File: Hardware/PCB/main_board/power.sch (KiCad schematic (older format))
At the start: 8 parts, among them J4 USB_B

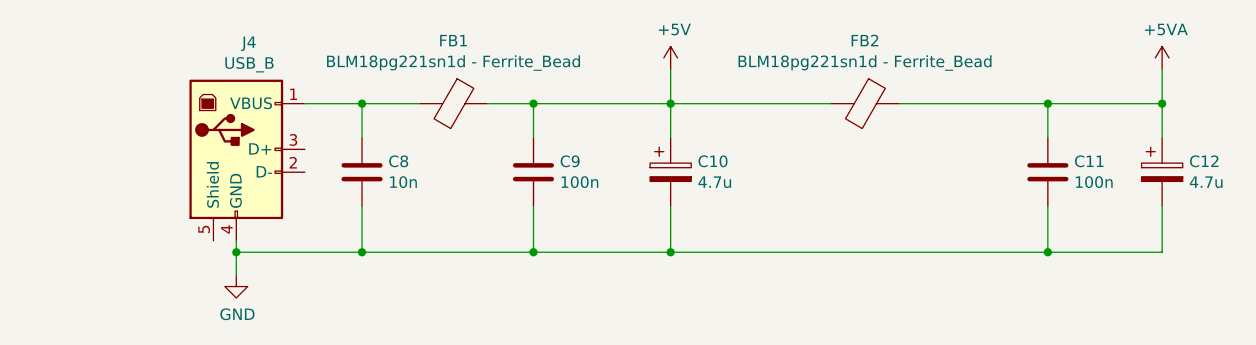
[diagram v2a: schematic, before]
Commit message: Update 3D view
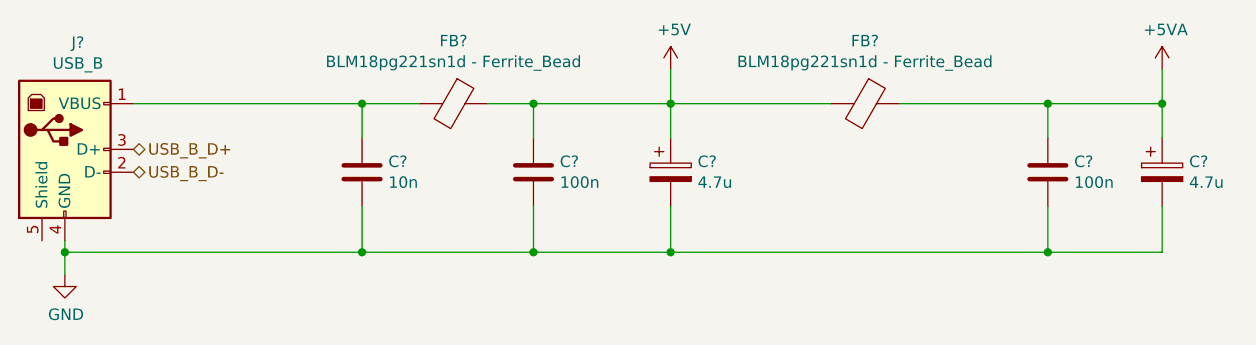
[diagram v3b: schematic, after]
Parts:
- renumbered C8 to C?, C9 to C?, C10 to C?, C11 to C?, C12 to C?, FB1 to FB?, FB2 to FB?, J4 to J?
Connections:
- net USB_B_D-: now reaches J?.2 (D-)
- net USB_B_D+: now reaches J?.3 (D+)
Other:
- moved on the sheet: J?
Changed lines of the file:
@@
 $Descr A4 11693 8268
 encoding utf-8
-Sheet 5 7
+Sheet 3 7
 Title ""
 Date ""
@@
 $EndDescr
 $Comp
-L power:GND #PWR09
+L power:GND #PWR?
 U 1 1 5E57CDA6
-P 2650 3650
-F 0 "#PWR09" H 2650 3400 50  0001 C CNN
-F 1 "GND" H 2655 3477 50  0000 C CNN
-F 2 "" H 2650 3650 50  0001 C CNN
-F 3 "" H 2650 3650 50  0001 C CNN
-	1    2650 3650
-	1    0    0    -1
-$EndComp
-$Comp
-L power:+5V #PWR010
+P 1900 3650
+F 0 "#PWR?" H 1900 3400 50  0001 C CNN
+F 1 "GND" H 1905 3477 50  0000 C CNN
+F 2 "" H 1900 3650 50  0001 C CNN
+F 3 "" H 1900 3650 50  0001 C CNN
+	1    1900 3650
+	1    0    0    -1
+$EndComp
+$Comp
+L power:+5V #PWR?
 U 1 1 5E57CEED
 P 4550 2750
-F 0 "#PWR010" H 4550 2600 50  0001 C CNN
+F 0 "#PWR?" H 4550 2600 50  0001 C CNN
 F 1 "+5V" H 4565 2923 50  0000 C CNN
 F 2 "" H 4550 2750 50  0001 C CNN
@@
 $EndComp
 $Comp
-L power:+5VA #PWR011
+L power:+5VA #PWR?
 U 1 1 5E57D330
 P 6700 2750
-F 0 "#PWR011" H 6700 2600 50  0001 C CNN
+F 0 "#PWR?" H 6700 2600 50  0001 C CNN
 F 1 "+5VA" H 6715 2923 50  0000 C CNN
 F 2 "" H 6700 2750 50  0001 C CNN
@@
 $EndComp
 $Comp
-L Device:Ferrite_Bead FB1
+L Device:Ferrite_Bead FB?
 U 1 1 5E57DA71
 P 3600 2900
-F 0 "FB1" V 3326 2900 50  0000 C CNN
+F 0 "FB?" V 3326 2900 50  0000 C CNN
 F 1 "BLM18pg221sn1d - Ferrite_Bead" V 3417 2900 50  0000 C CNN
 F 2 "Inductor_SMD:L_0603_1608Metric" V 3530 2900 50  0001 C CNN
@@
 $EndComp
 $Comp
-L Connector:USB_B J4
+L Connector:USB_B J?
 U 1 1 5E57F8C7
-P 2650 3100
-F 0 "J4" H 2707 3567 50  0000 C CNN
-F 1 "USB_B" H 2707 3476 50  0000 C CNN
-F 2 "Connector_USB:USB_B_OST_USB-B1HSxx_Horizontal" H 2800 3050 50  0001 C CNN
-F 3 " ~" H 2800 3050 50  0001 C CNN
-	1    2650 3100
-	1    0    0    -1
-$EndComp
-Wire Wire Line
-	2650 3650 2650 3550
-Wire Wire Line
-	2950 2900 3200 2900
+P 1900 3100
+F 0 "J?" H 1957 3567 50  0000 C CNN
+F 1 "USB_B" H 1957 3476 50  0000 C CNN
+F 2 "Connector_USB:USB_B_OST_USB-B1HSxx_Horizontal" H 2050 3050 50  0001 C CNN
+F 3 " ~" H 2050 3050 50  0001 C CNN
+	1    1900 3100
+	1    0    0    -1
+$EndComp
+Wire Wire Line
+	1900 3650 1900 3550
+Wire Wire Line
+	2200 2900 3200 2900
 Wire Wire Line
 	4550 2900 4550 2750
 Wire Wire Line
-	2650 3550 3200 3550
-Connection ~ 2650 3550
-Wire Wire Line
-	2650 3550 2650 3500
-$Comp
-L Device:C C8
+	1900 3550 3200 3550
+Connection ~ 1900 3550
+Wire Wire Line
+	1900 3550 1900 3500
+$Comp
+L Device:C C?
 U 1 1 5E583763
 P 3200 3200
-F 0 "C8" H 3315 3246 50  0000 L CNN
+F 0 "C?" H 3315 3246 50  0000 L CNN
 F 1 "10n" H 3315 3155 50  0000 L CNN
 F 2 "Capacitor_SMD:C_0805_2012Metric" H 3238 3050 50  0001 C CNN
@@
 $EndComp
 $Comp
-L Device:C C9
+L Device:C C?
 U 1 1 5E583C5A
 P 3950 3200
-F 0 "C9" H 4065 3246 50  0000 L CNN
+F 0 "C?" H 4065 3246 50  0000 L CNN
 F 1 "100n" H 4065 3155 50  0000 L CNN
 F 2 "Capacitor_SMD:C_0805_2012Metric" H 3988 3050 50  0001 C CNN
@@
 $EndComp
 $Comp
-L Device:CP C10
+L Device:CP C?
 U 1 1 5E584603
 P 4550 3200
-F 0 "C10" H 4668 3246 50  0000 L CNN
+F 0 "C?" H 4668 3246 50  0000 L CNN
 F 1 "4.7u" H 4668 3155 50  0000 L CNN
 F 2 "Capacitor_SMD:CP_Elec_4x5.4" H 4588 3050 50  0001 C CNN
@@
 	4550 3350 4550 3550
 $Comp
-L Device:Ferrite_Bead FB2
+L Device:Ferrite_Bead FB?
 U 1 1 5E587793
 P 5400 2900
-F 0 "FB2" V 5126 2900 50  0000 C CNN
+F 0 "FB?" V 5126 2900 50  0000 C CNN
 F 1 "BLM18pg221sn1d - Ferrite_Bead" V 5217 2900 50  0000 C CNN
 F 2 "Inductor_SMD:L_0603_1608Metric" V 5330 2900 50  0001 C CNN
@@
 	6700 2900 6700 2750
 $Comp
-L Device:C C11
+L Device:C C?
 U 1 1 5E58BFC4
 P 6200 3200
-F 0 "C11" H 6315 3246 50  0000 L CNN
+F 0 "C?" H 6315 3246 50  0000 L CNN
 F 1 "100n" H 6315 3155 50  0000 L CNN
 F 2 "Capacitor_SMD:C_0805_2012Metric" H 6238 3050 50  0001 C CNN
@@
 $EndComp
 $Comp
-L Device:CP C12
+L Device:CP C?
 U 1 1 5E58C4AF
 P 6700 3200
-F 0 "C12" H 6818 3246 50  0000 L CNN
+F 0 "C?" H 6818 3246 50  0000 L CNN
 F 1 "4.7u" H 6818 3155 50  0000 L CNN
 F 2 "Capacitor_SMD:CP_Elec_4x5.4" H 6738 3050 50  0001 C CNN
@@
 Wire Wire Line
 	6200 2900 6700 2900
+Text HLabel 2200 3100 2    50   BiDi ~ 0
+USB_B_D+
+Text HLabel 2200 3200 2    50   BiDi ~ 0
+USB_B_D-
 $EndSCHEMATC

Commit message: Route GPIO
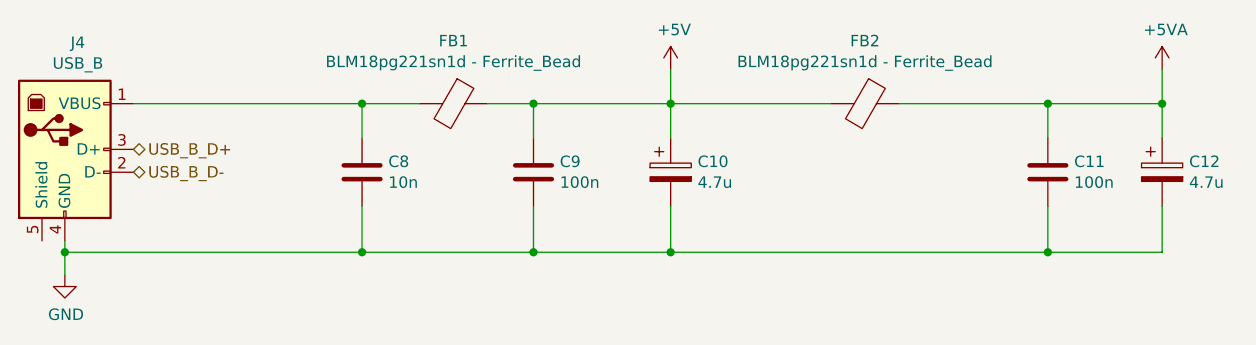
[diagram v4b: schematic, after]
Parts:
- gave numbers to parts that had none: 8
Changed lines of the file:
@@
 $EndDescr
 $Comp
-L power:GND #PWR?
+L power:GND #PWR0118
 U 1 1 5E57CDA6
 P 1900 3650
-F 0 "#PWR?" H 1900 3400 50  0001 C CNN
+F 0 "#PWR0118" H 1900 3400 50  0001 C CNN
 F 1 "GND" H 1905 3477 50  0000 C CNN
 F 2 "" H 1900 3650 50  0001 C CNN
@@
 $EndComp
 $Comp
-L power:+5V #PWR?
+L power:+5V #PWR0119
 U 1 1 5E57CEED
 P 4550 2750
-F 0 "#PWR?" H 4550 2600 50  0001 C CNN
+F 0 "#PWR0119" H 4550 2600 50  0001 C CNN
 F 1 "+5V" H 4565 2923 50  0000 C CNN
 F 2 "" H 4550 2750 50  0001 C CNN
@@
 $EndComp
 $Comp
-L power:+5VA #PWR?
+L power:+5VA #PWR0120
 U 1 1 5E57D330
 P 6700 2750
-F 0 "#PWR?" H 6700 2600 50  0001 C CNN
+F 0 "#PWR0120" H 6700 2600 50  0001 C CNN
 F 1 "+5VA" H 6715 2923 50  0000 C CNN
 F 2 "" H 6700 2750 50  0001 C CNN
@@
 $EndComp
 $Comp
-L Device:Ferrite_Bead FB?
+L Device:Ferrite_Bead FB1
 U 1 1 5E57DA71
 P 3600 2900
-F 0 "FB?" V 3326 2900 50  0000 C CNN
+F 0 "FB1" V 3326 2900 50  0000 C CNN
 F 1 "BLM18pg221sn1d - Ferrite_Bead" V 3417 2900 50  0000 C CNN
 F 2 "Inductor_SMD:L_0603_1608Metric" V 3530 2900 50  0001 C CNN
@@
 $EndComp
 $Comp
-L Connector:USB_B J?
+L Connector:USB_B J4
 U 1 1 5E57F8C7
 P 1900 3100
-F 0 "J?" H 1957 3567 50  0000 C CNN
+F 0 "J4" H 1957 3567 50  0000 C CNN
 F 1 "USB_B" H 1957 3476 50  0000 C CNN
 F 2 "Connector_USB:USB_B_OST_USB-B1HSxx_Horizontal" H 2050 3050 50  0001 C CNN
@@
 	1900 3550 1900 3500
 $Comp
-L Device:C C?
+L Device:C C8
 U 1 1 5E583763
 P 3200 3200
-F 0 "C?" H 3315 3246 50  0000 L CNN
+F 0 "C8" H 3315 3246 50  0000 L CNN
 F 1 "10n" H 3315 3155 50  0000 L CNN
 F 2 "Capacitor_SMD:C_0805_2012Metric" H 3238 3050 50  0001 C CNN
@@
 $EndComp
 $Comp
-L Device:C C?
+L Device:C C9
 U 1 1 5E583C5A
 P 3950 3200
-F 0 "C?" H 4065 3246 50  0000 L CNN
+F 0 "C9" H 4065 3246 50  0000 L CNN
 F 1 "100n" H 4065 3155 50  0000 L CNN
 F 2 "Capacitor_SMD:C_0805_2012Metric" H 3988 3050 50  0001 C CNN
@@
 $EndComp
 $Comp
-L Device:CP C?
+L Device:CP C10
 U 1 1 5E584603
 P 4550 3200
-F 0 "C?" H 4668 3246 50  0000 L CNN
+F 0 "C10" H 4668 3246 50  0000 L CNN
 F 1 "4.7u" H 4668 3155 50  0000 L CNN
 F 2 "Capacitor_SMD:CP_Elec_4x5.4" H 4588 3050 50  0001 C CNN
@@
 	4550 3350 4550 3550
 $Comp
-L Device:Ferrite_Bead FB?
+L Device:Ferrite_Bead FB2
 U 1 1 5E587793
 P 5400 2900
-F 0 "FB?" V 5126 2900 50  0000 C CNN
+F 0 "FB2" V 5126 2900 50  0000 C CNN
 F 1 "BLM18pg221sn1d - Ferrite_Bead" V 5217 2900 50  0000 C CNN
 F 2 "Inductor_SMD:L_0603_1608Metric" V 5330 2900 50  0001 C CNN
@@
 	6700 2900 6700 2750
 $Comp
-L Device:C C?
+L Device:C C11
 U 1 1 5E58BFC4
 P 6200 3200
-F 0 "C?" H 6315 3246 50  0000 L CNN
+F 0 "C11" H 6315 3246 50  0000 L CNN
 F 1 "100n" H 6315 3155 50  0000 L CNN
 F 2 "Capacitor_SMD:C_0805_2012Metric" H 6238 3050 50  0001 C CNN
@@
 $EndComp
 $Comp
-L Device:CP C?
+L Device:CP C12
 U 1 1 5E58C4AF
 P 6700 3200
-F 0 "C?" H 6818 3246 50  0000 L CNN
+F 0 "C12" H 6818 3246 50  0000 L CNN
 F 1 "4.7u" H 6818 3155 50  0000 L CNN
 F 2 "Capacitor_SMD:CP_Elec_4x5.4" H 6738 3050 50  0001 C CNN

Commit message: Route PWR
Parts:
- FB1, FB2: value BLM18pg221sn1d - Ferrite_Bead -> BLM21PG221SH1D - Ferrite_Bead; footprint Inductor_SMD:L_0603_1608Metric -> Inductor_SMD:L_0805_2012Metric
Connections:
- net PWR_RAW: now reaches C8.1, FB1.2, J4.1 (VBUS)
- no-connect marks 0 -> 1
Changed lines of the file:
@@
 P 3600 2900
 F 0 "FB1" V 3326 2900 50  0000 C CNN
-F 1 "BLM18pg221sn1d - Ferrite_Bead" V 3417 2900 50  0000 C CNN
-F 2 "Inductor_SMD:L_0603_1608Metric" V 3530 2900 50  0001 C CNN
+F 1 "BLM21PG221SH1D - Ferrite_Bead" V 3417 2900 50  0000 C CNN
+F 2 "Inductor_SMD:L_0805_2012Metric" V 3530 2900 50  0001 C CNN
 F 3 "~" H 3600 2900 50  0001 C CNN
 	1    3600 2900
@@
 P 5400 2900
 F 0 "FB2" V 5126 2900 50  0000 C CNN
-F 1 "BLM18pg221sn1d - Ferrite_Bead" V 5217 2900 50  0000 C CNN
-F 2 "Inductor_SMD:L_0603_1608Metric" V 5330 2900 50  0001 C CNN
+F 1 "BLM21PG221SH1D - Ferrite_Bead" V 5217 2900 50  0000 C CNN
+F 2 "Inductor_SMD:L_0805_2012Metric" V 5330 2900 50  0001 C CNN
 F 3 "~" H 5400 2900 50  0001 C CNN
 	1    5400 2900
@@
 Wire Wire Line
 	6200 2900 6700 2900
+NoConn ~ 1800 3500
 Text HLabel 2200 3100 2    50   BiDi ~ 0
 USB_B_D+
 Text HLabel 2200 3200 2    50   BiDi ~ 0
 USB_B_D-
+Text Label 2300 2900 0    50   ~ 0
+PWR_RAW
 $EndSCHEMATC

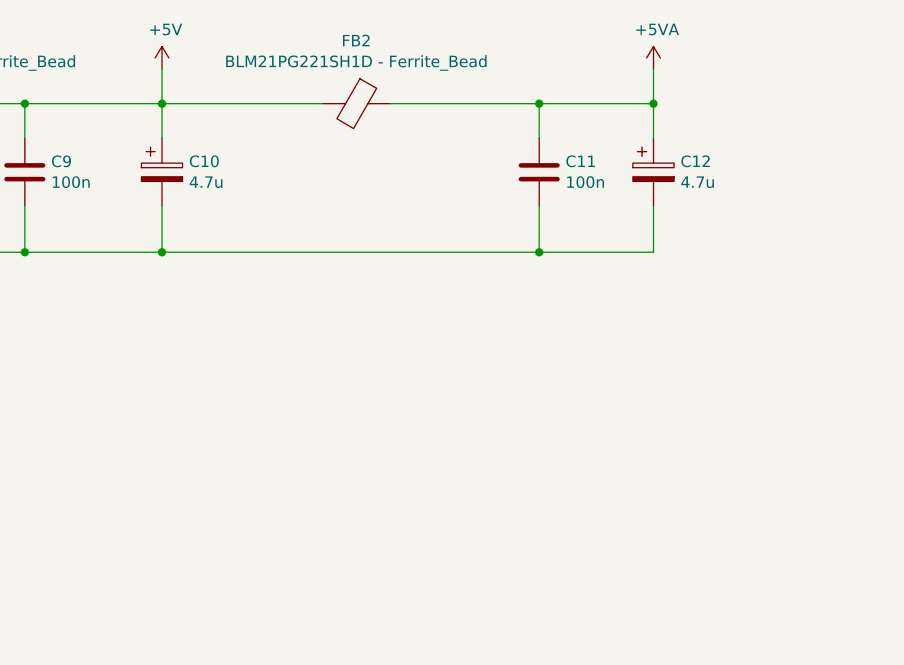
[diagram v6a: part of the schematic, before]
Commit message: Add test points headers
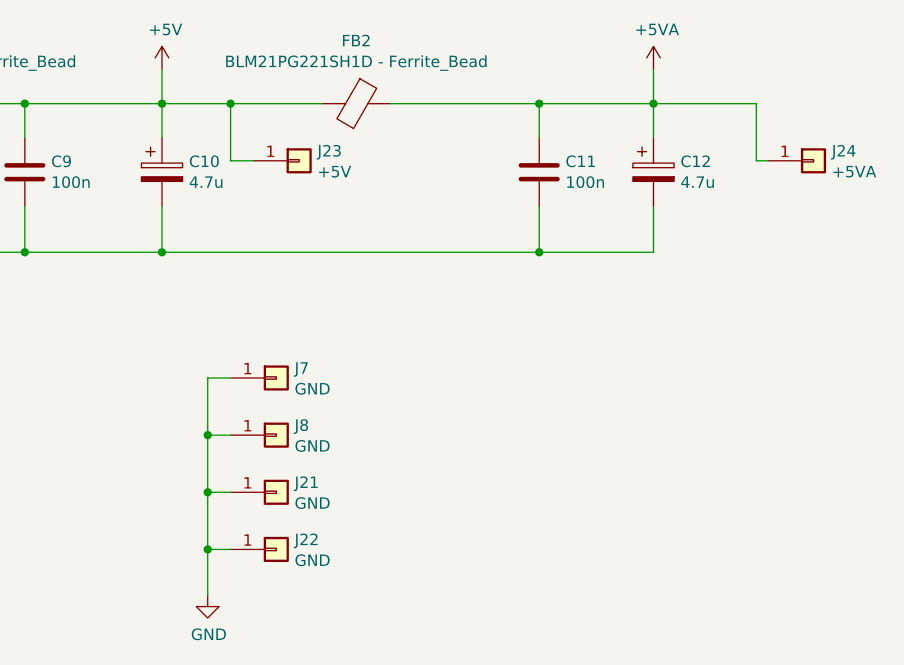
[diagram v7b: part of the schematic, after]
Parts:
- added J21, J22, J7, J8: GND, Connector_PinHeader_2.54mm:PinHeader_1x01_P2.54mm_Vertical, symbol Connector_Generic:Conn_01x01
- added J23: +5V, Connector_PinHeader_2.54mm:PinHeader_1x01_P2.54mm_Vertical, symbol Connector_Generic:Conn_01x01
- added J24: +5VA, Connector_PinHeader_2.54mm:PinHeader_1x01_P2.54mm_Vertical, symbol Connector_Generic:Conn_01x01
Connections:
- net +5V: now also J23.1 (Pin_1)
- net +5VA: now also J24.1 (Pin_1)
- net GND: now also J21.1 (Pin_1), J22.1 (Pin_1), J7.1 (Pin_1), J8.1 (Pin_1)
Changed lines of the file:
@@
 $EndComp
 Wire Wire Line
-	4550 2900 5250 2900
+	4550 2900 4850 2900
 Wire Wire Line
 	5550 2900 6200 2900
@@
 $EndComp
 Wire Wire Line
-	4550 3550 6200 3550
-Wire Wire Line
 	6200 3550 6200 3350
 Connection ~ 4550 3550
@@
 Text Label 2300 2900 0    50   ~ 0
 PWR_RAW
+Wire Wire Line
+	4950 3150 4850 3150
+Wire Wire Line
+	4850 3150 4850 2900
+Connection ~ 4850 2900
+Wire Wire Line
+	4850 2900 5250 2900
+Wire Wire Line
+	7150 2900 7150 3150
+Wire Wire Line
+	7150 3150 7200 3150
+Wire Wire Line
+	6700 2900 7150 2900
+Wire Wire Line
+	4550 3550 6200 3550
+$Comp
+L Connector_Generic:Conn_01x01 J23
+U 1 1 5E8B96CD
+P 5150 3150
+F 0 "J23" H 5230 3192 50  0000 L CNN
+F 1 "+5V" H 5230 3101 50  0000 L CNN
+F 2 "Connector_PinHeader_2.54mm:PinHeader_1x01_P2.54mm_Vertical" H 5150 3150 50  0001 C CNN
+F 3 "~" H 5150 3150 50  0001 C CNN
+	1    5150 3150
+	1    0    0    -1
+$EndComp
+$Comp
+L Connector_Generic:Conn_01x01 J24
+U 1 1 5E8BB0B1
+P 7400 3150
+F 0 "J24" H 7480 3192 50  0000 L CNN
+F 1 "+5VA" H 7480 3101 50  0000 L CNN
+F 2 "Connector_PinHeader_2.54mm:PinHeader_1x01_P2.54mm_Vertical" H 7400 3150 50  0001 C CNN
+F 3 "~" H 7400 3150 50  0001 C CNN
+	1    7400 3150
+	1    0    0    -1
+$EndComp
+$Comp
+L Connector_Generic:Conn_01x01 J7
+U 1 1 5E8BB863
+P 5050 4100
+F 0 "J7" H 5130 4142 50  0000 L CNN
+F 1 "GND" H 5130 4051 50  0000 L CNN
+F 2 "Connector_PinHeader_2.54mm:PinHeader_1x01_P2.54mm_Vertical" H 5050 4100 50  0001 C CNN
+F 3 "~" H 5050 4100 50  0001 C CNN
+	1    5050 4100
+	1    0    0    -1
+$EndComp
+$Comp
+L Connector_Generic:Conn_01x01 J8
+U 1 1 5E8BBAF1
+P 5050 4350
+F 0 "J8" H 5130 4392 50  0000 L CNN
+F 1 "GND" H 5130 4301 50  0000 L CNN
+F 2 "Connector_PinHeader_2.54mm:PinHeader_1x01_P2.54mm_Vertical" H 5050 4350 50  0001 C CNN
+F 3 "~" H 5050 4350 50  0001 C CNN
+	1    5050 4350
+	1    0    0    -1
+$EndComp
+$Comp
+L Connector_Generic:Conn_01x01 J21
+U 1 1 5E8BBE17
+P 5050 4600
+F 0 "J21" H 5130 4642 50  0000 L CNN
+F 1 "GND" H 5130 4551 50  0000 L CNN
+F 2 "Connector_PinHeader_2.54mm:PinHeader_1x01_P2.54mm_Vertical" H 5050 4600 50  0001 C CNN
+F 3 "~" H 5050 4600 50  0001 C CNN
+	1    5050 4600
+	1    0    0    -1
+$EndComp
+$Comp
+L Connector_Generic:Conn_01x01 J22
+U 1 1 5E8BC08F
+P 5050 4850
+F 0 "J22" H 5130 4892 50  0000 L CNN
+F 1 "GND" H 5130 4801 50  0000 L CNN
+F 2 "Connector_PinHeader_2.54mm:PinHeader_1x01_P2.54mm_Vertical" H 5050 4850 50  0001 C CNN
+F 3 "~" H 5050 4850 50  0001 C CNN
+	1    5050 4850
+	1    0    0    -1
+$EndComp
+Wire Wire Line
+	4850 4100 4750 4100
+Wire Wire Line
+	4750 4100 4750 4350
+Wire Wire Line
+	4750 4850 4850 4850
+Wire Wire Line
+	4850 4600 4750 4600
+Connection ~ 4750 4600
+Wire Wire Line
+	4750 4600 4750 4850
+Wire Wire Line
+	4850 4350 4750 4350
+Connection ~ 4750 4350
+Wire Wire Line
+	4750 4350 4750 4600
+Wire Wire Line
+	4750 4850 4750 5050
+Connection ~ 4750 4850
+$Comp
+L power:GND #PWR0134
+U 1 1 5E8BEA10
+P 4750 5050
+F 0 "#PWR0134" H 4750 4800 50  0001 C CNN
+F 1 "GND" H 4755 4877 50  0000 C CNN
+F 2 "" H 4750 5050 50  0001 C CNN
+F 3 "" H 4750 5050 50  0001 C CNN
+	1    4750 5050
+	1    0    0    -1
+$EndComp
 $EndSCHEMATC
